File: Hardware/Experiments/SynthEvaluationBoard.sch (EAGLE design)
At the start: 174 parts, among them IC1 STW81200, IC19 AP2114H, IC2 AD9913, IC3 NCP702-1.8, IC34 NCP702-1.8, IC4 SI5332A-GM1, IC5 STM32L462CE, J1 AMPHENOL_901-10510-2, J2 AMPHENOL_901-10510-2, J3 AMPHENOL_901-10510-2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

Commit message: Minor adjustments + gerbers
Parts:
- added LED1, LED2, LED3, LED4, LED5: Green, eagle-ltspice:LED_ESML0603
- added R52: 470, VNA:R-EU_R0402
- added R53, R54, R55, R56: 220, VNA:R-EU_R0402
- R46: value 10k -> 1k
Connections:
- new net N$48: LED3.A, R52.1
- new net N$50: LED1.A, R53.1
- new net N$52: LED2.A, R54.1
- new net N$53: LED4.A, R55.1
- new net N$65: LED5.A, R56.1
- new net N$81: IC5.PA3, R53.2
- new net N$82: IC5.PA2, R54.2
- new net N$83: IC5.PA1, R55.2
- new net N$84: IC5.PA0, R56.2
- net +5V: now also R52.2
- net GND: now also LED1.C, LED2.C, LED3.C, LED4.C, LED5.C
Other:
- moved on the sheet: C64, C65, C66, C67, C68, IC5, JP10, JP12, JP9, R26, R47, R48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

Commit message: Added milling layer to gerber, created BOM
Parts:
- R23, R24: value (none) -> 49R9
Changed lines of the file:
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@@
 <part name="J1" library="VNA" library_urn="urn:adsk.eagle:library:22367181" deviceset="AMPHENOL_901-10510-2" device=""/>
 <part name="GND16" library="VNA" library_urn="urn:adsk.eagle:library:22367181" deviceset="GND" device=""/>
-<part name="R23" library="VNA" library_urn="urn:adsk.eagle:library:22367181" deviceset="R-EU_" device="R0402" package3d_urn="urn:adsk.eagle:package:22367274/3"/>
+<part name="R23" library="VNA" library_urn="urn:adsk.eagle:library:22367181" deviceset="R-EU_" device="R0402" package3d_urn="urn:adsk.eagle:package:22367274/3" value="49R9"/>
 <part name="GND37" library="VNA" library_urn="urn:adsk.eagle:library:22367181" deviceset="GND" device=""/>
 <part name="J2" library="VNA" library_urn="urn:adsk.eagle:library:22367181" deviceset="AMPHENOL_901-10510-2" device=""/>
@@
 <part name="J6" library="VNA" library_urn="urn:adsk.eagle:library:22367181" deviceset="BU-1420701851" device=""/>
 <part name="GND42" library="VNA" library_urn="urn:adsk.eagle:library:22367181" deviceset="GND" device=""/>
-<part name="R24" library="VNA" library_urn="urn:adsk.eagle:library:22367181" deviceset="R-EU_" device="R0402" package3d_urn="urn:adsk.eagle:package:22367274/3"/>
+<part name="R24" library="VNA" library_urn="urn:adsk.eagle:library:22367181" deviceset="R-EU_" device="R0402" package3d_urn="urn:adsk.eagle:package:22367274/3" value="49R9"/>
 <part name="GND43" library="VNA" library_urn="urn:adsk.eagle:library:22367181" deviceset="GND" device=""/>
 <part name="GND44" library="VNA" library_urn="urn:adsk.eagle:library:22367181" deviceset="GND" device=""/>

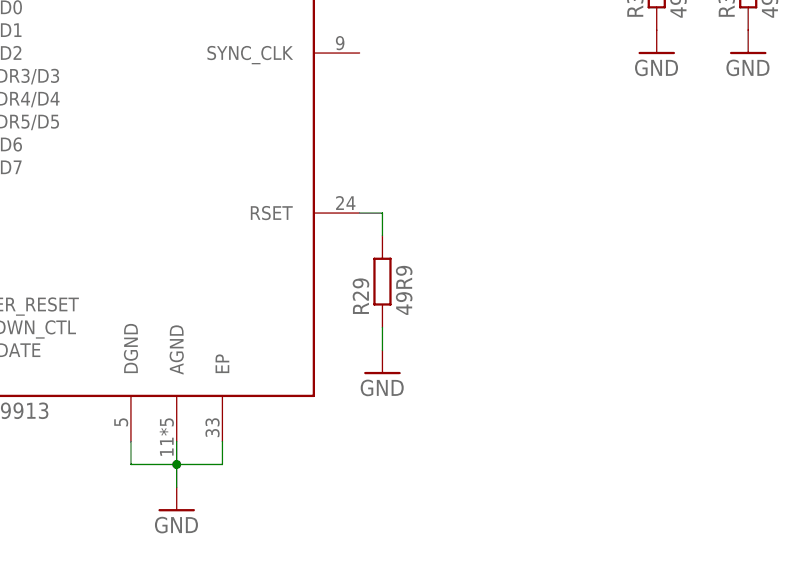
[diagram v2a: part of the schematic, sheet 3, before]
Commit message: minimal working Si5332/AD9913
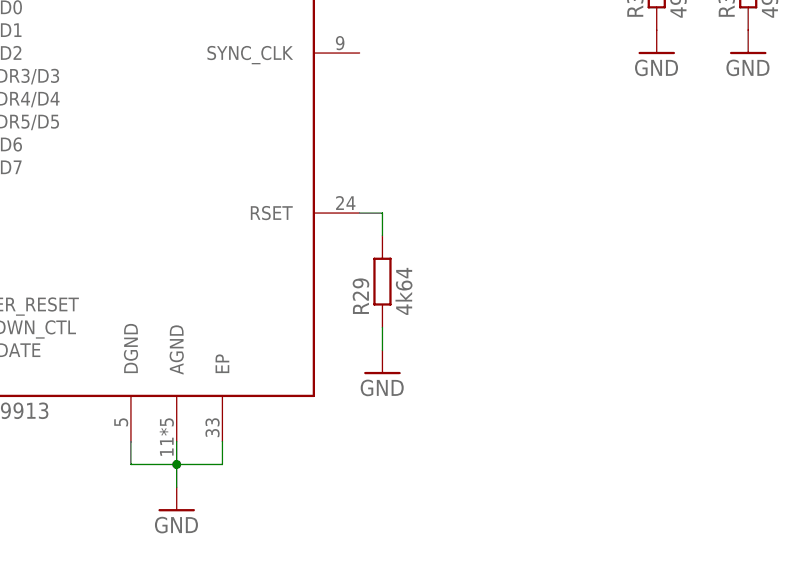
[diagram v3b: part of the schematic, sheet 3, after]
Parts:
- R29: value 49R9 -> 4k64
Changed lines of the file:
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@@
 <part name="IC2" library="VNA" library_urn="urn:adsk.eagle:library:22367181" deviceset="AD9913" device="" package3d_urn="urn:adsk.eagle:package:22367293/2"/>
 <part name="GND45" library="VNA" library_urn="urn:adsk.eagle:library:22367181" deviceset="GND" device=""/>
-<part name="R29" library="VNA" library_urn="urn:adsk.eagle:library:22367181" deviceset="R-EU_" device="R0402" package3d_urn="urn:adsk.eagle:package:22367274/3" value="49R9"/>
+<part name="R29" library="VNA" library_urn="urn:adsk.eagle:library:22367181" deviceset="R-EU_" device="R0402" package3d_urn="urn:adsk.eagle:package:22367274/3" value="4k64"/>
 <part name="GND46" library="VNA" library_urn="urn:adsk.eagle:library:22367181" deviceset="GND" device=""/>
 <part name="R30" library="VNA" library_urn="urn:adsk.eagle:library:22367181" deviceset="R-EU_" device="R0402" package3d_urn="urn:adsk.eagle:package:22367274/3" value="49R9"/>
